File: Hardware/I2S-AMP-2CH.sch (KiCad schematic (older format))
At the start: 19 parts, among them U7 TAS5760MDCAR

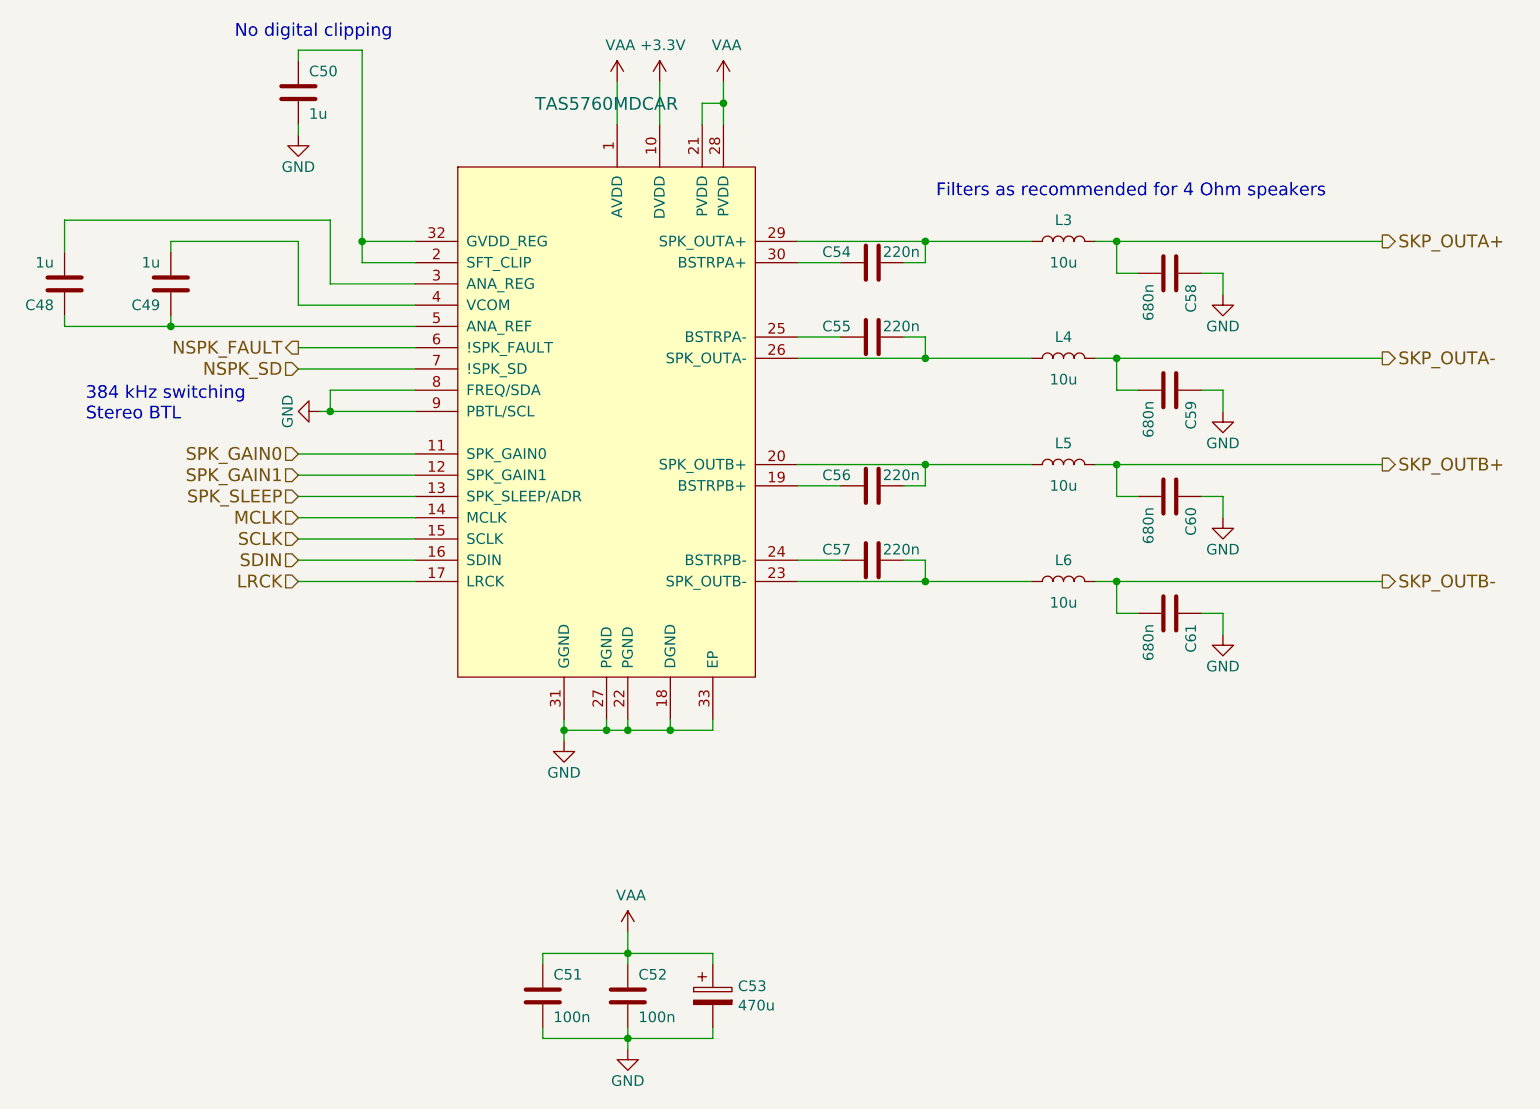
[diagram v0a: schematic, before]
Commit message: connect pi i2c to header
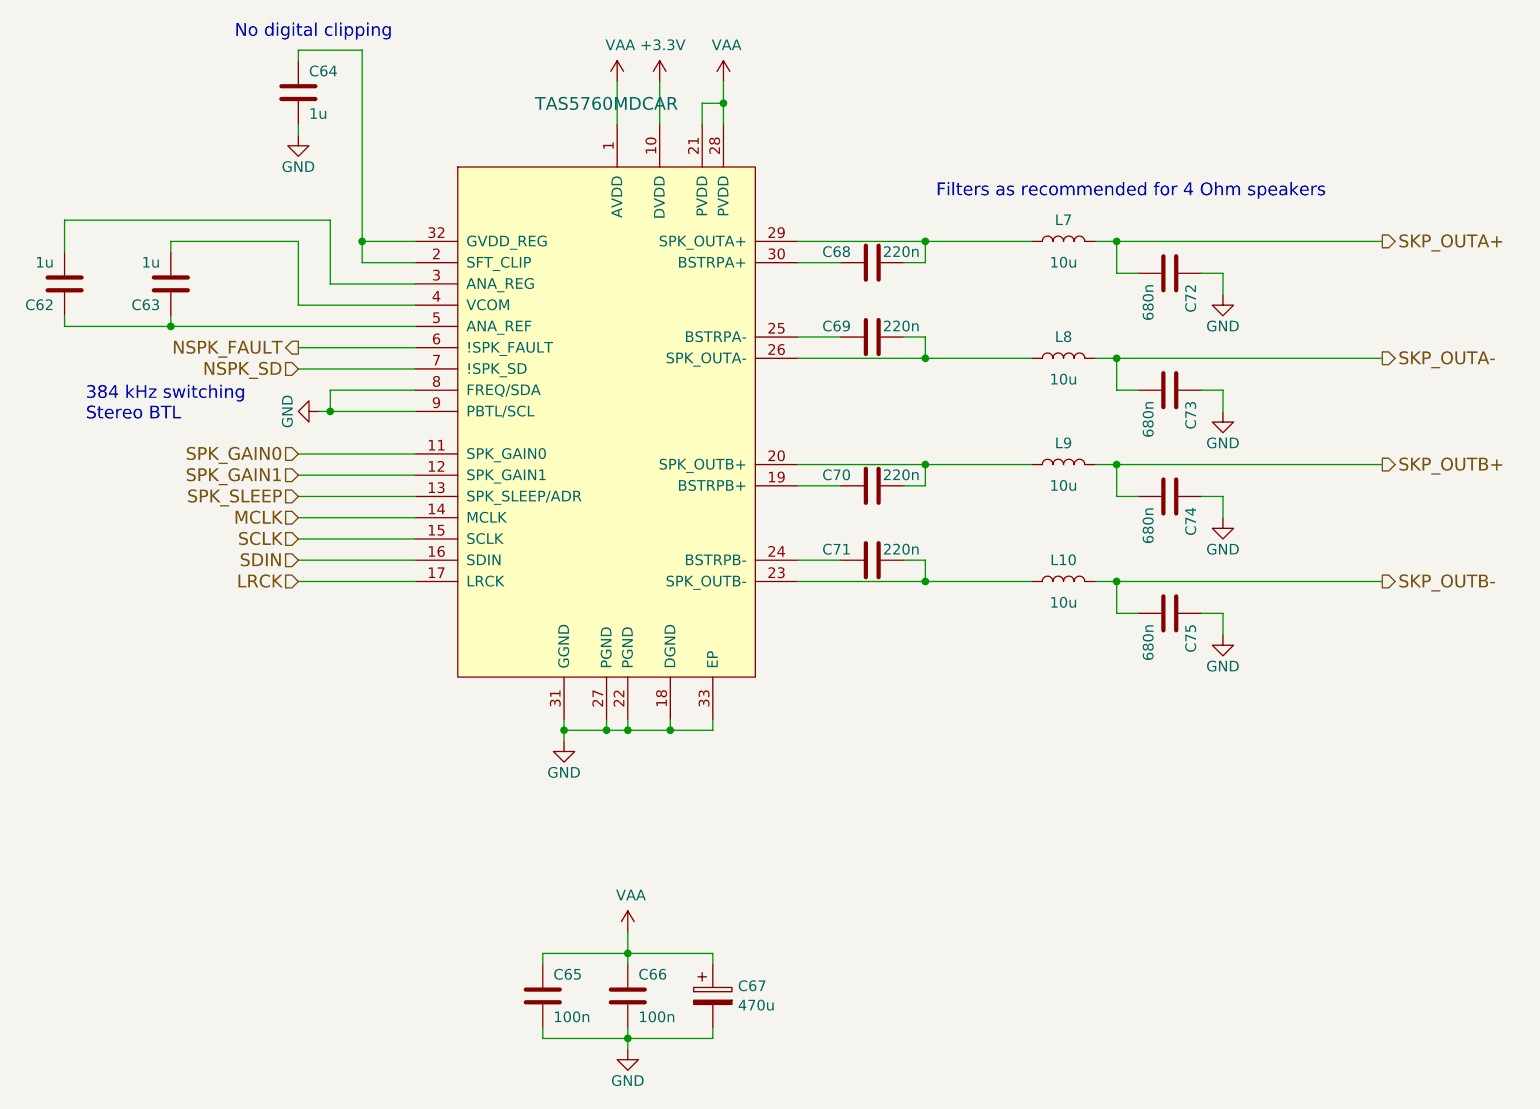
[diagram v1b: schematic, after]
